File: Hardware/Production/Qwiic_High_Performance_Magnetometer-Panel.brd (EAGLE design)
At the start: 99.3 x 93.9 mm, 420 parts, among them J1 Qwiic, J10 Qwiic, J11 Qwiic, J13 Qwiic, J14 Qwiic, J16 Qwiic, J17 Qwiic, J19 Qwiic, J2 Qwiic, J20 Qwiic, J22 Qwiic, J23 Qwiic, J25 Qwiic, J26 Qwiic, J4 Qwiic, J5 Qwiic, J7 Qwiic, J8 Qwiic, U1 MMC5893MA_QFN16, U2 MMC5893MA_QFN16, U3 MMC5893MA_QFN16, U4 MMC5893MA_QFN16, U5 MMC5893MA_QFN16, U6 MMC5893MA_QFN16, U7 MMC5893MA_QFN16, U8 MMC5893MA_QFN16, U9 MMC5893MA_QFN16

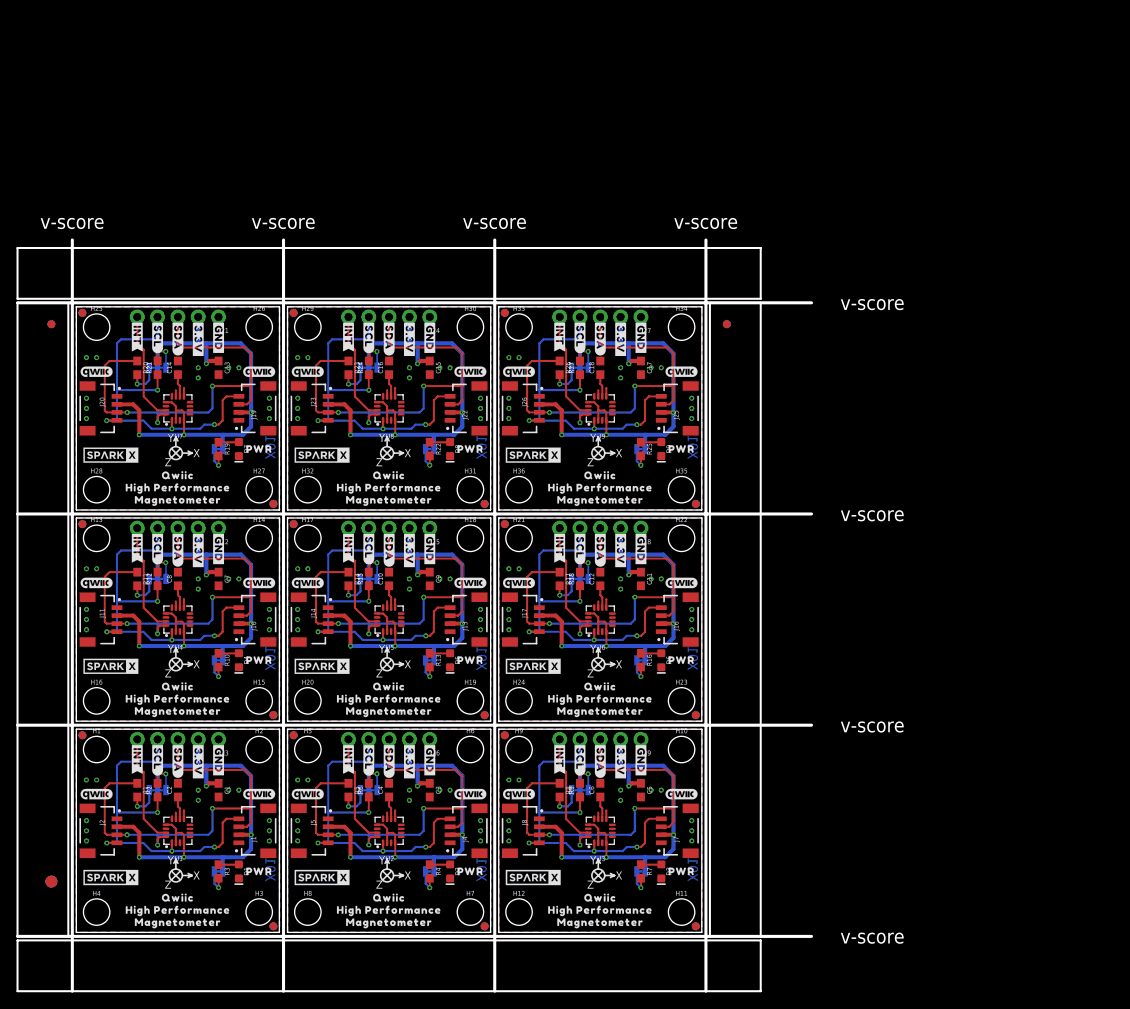
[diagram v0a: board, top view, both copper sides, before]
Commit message: Added SPI breakout header; created PCB production files.
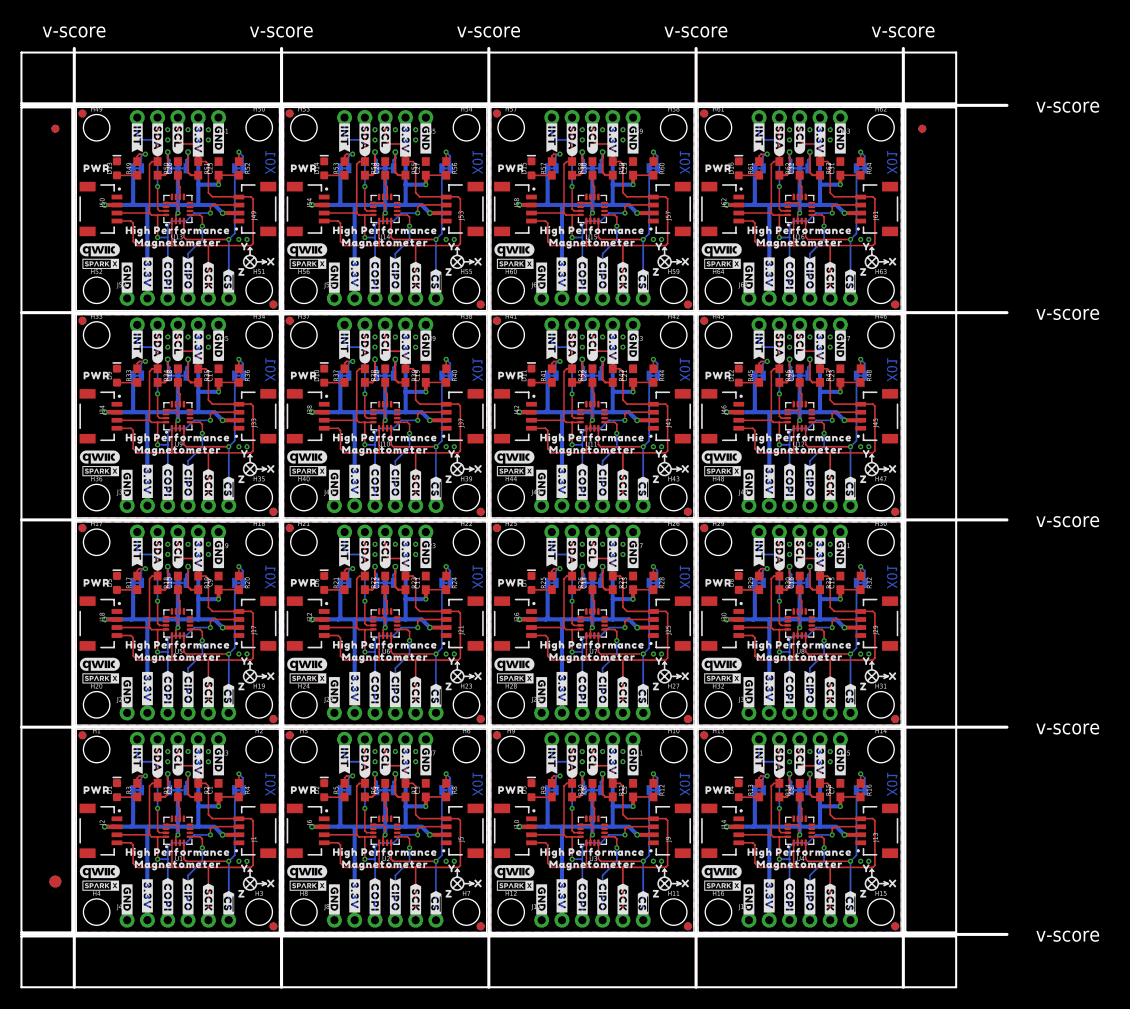
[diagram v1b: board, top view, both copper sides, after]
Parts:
- added C19, C21, C23, C25, C27, C29, C31: 0.1uF, SparkFun-Capacitors:0603
- added C20, C22, C24, C26, C28, C30, C32: 10uF, SparkFun-Capacitors:0603
- added D10, D11, D12, D13, D14, D15, D16: RED, SparkFun-LED:LED-0603
- added FD37, FD38, FD39, FD40, FD41, FD42, FD43, FD44, FD45, FD46, FD47, FD48, FD49, FD50, FD51, FD52, FD53, FD54, FD55, FD56, FD57, FD58, FD59, FD60, FD61, FD62, FD63, FD64: FIDUCIAL1X2, SparkFun-Aesthetics:FIDUCIAL-1X2
- added FRAME10, FRAME11, FRAME12, FRAME13, FRAME14, FRAME15, FRAME16: FRAME-LETTERNO_PACKAGE, SparkFun-Aesthetics:DUMMY
- added H37, H38, H39, H40, H41, H42, H43, H44, H45, H46, H47, H48, H49, H50, H51, H52, H53, H54, H55, H56, H57, H58, H59, H60, H61, H62, H63, H64: STAND-OFF, SparkFun-Hardware:STAND-OFF
- added J28, J32, J36, J40, J44, J48, J52, J56, J60, J64: (no value), SparkFun-Connectors:1X06_NO_SILK
- added J29, J30, J33, J34, J37, J38, J41, J42, J45, J46, J49, J50, J53, J54, J57, J58, J61, J62: Qwiic, SparkFun-Connectors:JST04_1MM_RA
- added J31, J35, J39, J43, J47, J51, J55, J59, J63: (no value), SparkFun-Connectors:1X05_NO_SILK
- added JP19, JP21, JP22, JP24, JP25, JP27, JP28, JP30, JP31, JP33, JP34, JP36, JP37, JP39, JP40, JP42, JP43, JP45, JP46, JP48: JUMPER-SMT_2_NC_TRACE_SILK, SparkFun-Jumpers:SMT-JUMPER_2_NC_TRACE_SILK
- added JP20, JP23, JP26, JP29, JP32, JP35, JP38, JP41, JP44, JP47: JUMPER-SMT_3_2-NC_TRACE_SILK, SparkFun-Jumpers:SMT-JUMPER_3_2-NC_TRACE_SILK
- added LOGO28, LOGO31, LOGO34, LOGO37, LOGO40, LOGO43, LOGO46: OSHW-LOGOMINI, SparkFun-Aesthetics:OSHW-LOGO-MINI
- added LOGO29, LOGO30, LOGO32, LOGO33, LOGO35, LOGO36, LOGO38, LOGO39, LOGO41, LOGO42, LOGO44, LOGO45, LOGO47, LOGO48: QWIIC_LOGO_5MM, SparkFun-Aesthetics:QWIIC_5MM
- added R28, R32, R36, R40, R44, R48, R52, R56, R60, R64: 10k, SparkFun-Resistors:0603
- added R29, R33, R37, R41, R45, R49, R53, R57, R61: 1k, SparkFun-Resistors:0603
- added R30, R31, R34, R35, R38, R39, R42, R43, R46, R47, R50, R51, R54, R55, R58, R59, R62, R63: 2.2k, SparkFun-Resistors:0603
- added U$199, U$238, U$277, U$316, U$355, U$394, U$433, U$472, U$511, U$550, U$589: (no value), output:PWR9
- added U$200, U$221, U$239, U$260, U$278, U$299, U$317, U$338, U$356, U$377, U$395, U$416, U$434, U$455, U$473, U$494, U$512, U$533, U$551, U$572, U$590, U$611: (no value), output:HIGH_PERFORMANCE11
- added U$201, U$222, U$240, U$261, U$279, U$300, U$318, U$339, U$357, U$378, U$396, U$417, U$435, U$456, U$474, U$495, U$513, U$534, U$552, U$573, U$591, U$612: (no value), output:MAGNETOMETER12
- added U$202, U$214, U$224, U$235, U$241, U$253, U$263, U$274, U$280, U$292, U$302, U$313, U$319, U$331, U$341, U$352, U$358, U$370, U$380, U$391, U$397, U$409, U$419, U$430, U$436, U$448, U$458, U$469, U$475, U$487, U$497, U$508, U$514, U$526, U$536, U$547, U$553, U$565, U$575, U$586, U$592, U$604, U$614: (no value), output:#3#3V#0
- added U$203, U$220, U$223, U$236, U$242, U$259, U$262, U$275, U$281, U$298, U$301, U$314, U$320, U$337, U$340, U$353, U$359, U$376, U$379, U$392, U$398, U$415, U$418, U$431, U$437, U$454, U$457, U$470, U$476, U$493, U$496, U$509, U$515, U$532, U$535, U$548, U$554, U$571, U$574, U$587, U$593, U$610, U$613: (no value), output:#GND#4
- added U$204, U$237, U$243, U$276, U$282, U$315, U$321, U$354, U$360, U$393, U$399, U$432, U$438, U$471, U$477, U$510, U$516, U$549, U$555, U$588, U$594: (no value), output:#INT#7
- added U$205, U$244, U$283, U$322, U$361, U$400, U$439, U$478, U$517, U$556, U$595: (no value), output:#LED#8
- added U$206, U$245, U$284, U$323, U$362, U$401, U$440, U$479, U$518, U$557, U$596: (no value), output:#I2C#9
- added U$207, U$246, U$285, U$324, U$363, U$402, U$441, U$480, U$519, U$558, U$597: (no value), output:#SPI#9
- added U$208, U$232, U$247, U$271, U$286, U$310, U$325, U$349, U$364, U$388, U$403, U$427, U$442, U$466, U$481, U$505, U$520, U$544, U$559, U$583, U$598, U$622: (no value), output:#SCL#6
- added U$209, U$233, U$248, U$272, U$287, U$311, U$326, U$350, U$365, U$389, U$404, U$428, U$443, U$467, U$482, U$506, U$521, U$545, U$560, U$584, U$599, U$623: (no value), output:#SDA#5
- added U$210, U$226, U$249, U$265, U$288, U$304, U$327, U$343, U$366, U$382, U$405, U$421, U$444, U$460, U$483, U$499, U$522, U$538, U$561, U$577, U$600, U$616: (no value), output:#CIPO#11
- added U$211, U$225, U$250, U$264, U$289, U$303, U$328, U$342, U$367, U$381, U$406, U$420, U$445, U$459, U$484, U$498, U$523, U$537, U$562, U$576, U$601, U$615: (no value), output:#COPI#12
- added U$212, U$227, U$251, U$266, U$290, U$305, U$329, U$344, U$368, U$383, U$407, U$422, U$446, U$461, U$485, U$500, U$524, U$539, U$563, U$578, U$602, U$617: (no value), output:#SCK#13
- added U$213, U$228, U$252, U$267, U$291, U$306, U$330, U$345, U$369, U$384, U$408, U$423, U$447, U$462, U$486, U$501, U$525, U$540, U$564, U$579, U$603, U$618: (no value), output:##CS##10
- added U$215, U$218, U$254, U$257, U$293, U$296, U$332, U$335, U$371, U$374, U$410, U$413, U$449, U$452, U$488, U$491, U$527, U$530, U$566, U$569, U$605, U$608: (no value), output:Y16
- added U$216, U$217, U$255, U$256, U$294, U$295, U$333, U$334, U$372, U$373, U$411, U$412, U$450, U$451, U$489, U$490, U$528, U$529, U$567, U$568, U$606, U$607: (no value), output:X15
- added U$219, U$234, U$258, U$273, U$297, U$312, U$336, U$351, U$375, U$390, U$414, U$429, U$453, U$468, U$492, U$507, U$531, U$546, U$570, U$585, U$609, U$624: (no value), output:Z17
- added U$229, U$268, U$307, U$346, U$385, U$424, U$463, U$502, U$541, U$580, U$619: SPARKX-LOGO2, SparkX:SPARKX-TINY
- added U$230, U$269, U$308, U$347, U$386, U$425, U$464, U$503, U$542, U$581, U$620: SPARKX-LOGO3, SparkX:SPARKX-SMALL
- added U$231, U$270, U$309, U$348, U$387, U$426, U$465, U$504, U$543, U$582, U$621: (no value), output:MADE_IN_THE_USA20
- added U10, U11, U12, U13, U14, U15, U16: MMC5893MA_QFN16, SparkFun-Sensors:LGA-16-3X3MM-4X4PINS
- J11, J19, J23, J7: value Qwiic -> (none); device SparkFun-Connectors:JST04_1MM_RA -> SparkFun-Connectors:1X05_NO_SILK
- J12, J24: device SparkFun-Connectors:1X05_NO_SILK -> SparkFun-Connectors:1X06_NO_SILK
- J16, J20, J4, J8: value Qwiic -> (none); device SparkFun-Connectors:JST04_1MM_RA -> SparkFun-Connectors:1X06_NO_SILK
- J18, J21, J6, J9: value (none) -> Qwiic; device SparkFun-Connectors:1X05_NO_SILK -> SparkFun-Connectors:JST04_1MM_RA
- JP10, JP12, JP16, JP18, JP4, JP6: value JUMPER-SMT_3_2-NC_TRACE_SILK -> JUMPER-SMT_2_NC_TRACE_SILK; device SparkFun-Jumpers:SMT-JUMPER_3_2-NC_TRACE_SILK -> SparkFun-Jumpers:SMT-JUMPER_2_NC_TRACE_SILK
- JP11, JP17, JP5: value JUMPER-SMT_2_NC_TRACE_SILK -> JUMPER-SMT_3_2-NC_TRACE_SILK; device SparkFun-Jumpers:SMT-JUMPER_2_NC_TRACE_SILK -> SparkFun-Jumpers:SMT-JUMPER_3_2-NC_TRACE_SILK
- LOGO11, LOGO12, LOGO14, LOGO15, LOGO17, LOGO18, LOGO2, LOGO20, LOGO21, LOGO23, LOGO24, LOGO26, LOGO27, LOGO3, LOGO5, LOGO6, LOGO8, LOGO9: value QWIIC_LOGO_4MM -> QWIIC_LOGO_5MM; device SparkFun-Aesthetics:QWIIC_4MM -> SparkFun-Aesthetics:QWIIC_5MM
- R10, R19, R22, R7: value 1k -> 2.2k
- R12, R20, R24, R8: value 2.2k -> 10k
- R16, R4: value 1k -> 10k
- R17, R21, R5, R9: value 2.2k -> 1k
- U$1: value SPARKX-LOGO5 -> (none); device SparkX:SPARKX-LARGE -> output:HIGH_PERFORMANCE11
- U$100, U$25: device output:#3#3V#0 -> output:X15
- U$101, U$26: device output:#GND#4 -> output:Y16
- U$102, U$27: device output:#SCL#6 -> output:Z17
- U$103, U$125, U$28: device output:#SDA#5 -> output:#GND#4
- U$104, U$161: device output:#INT#7 -> output:HIGH_PERFORMANCE11
- U$105: device output:QWIIC10 -> output:MAGNETOMETER12
- U$106, U$142, U$164: device output:HIGH_PERFORMANCE11 -> output:#GND#4
- U$107, U$85: device output:MAGNETOMETER12 -> output:#3#3V#0
- U$108: device output:MADE_IN_THE_USA13 -> output:#COPI#12
- U$109: device output:#LED#8 -> output:#CIPO#11
- U$110: device output:#I2C#9 -> output:#SCK#13
- U$111: value SPARKX-LOGO5 -> (none); device SparkX:SPARKX-LARGE -> output:##CS##10
- U$112: value SPARKX-LOGO3 -> SPARKX-LOGO2; device SparkX:SPARKX-SMALL -> SparkX:SPARKX-TINY
- U$113: value (none) -> SPARKX-LOGO3; device output:#3#3V#0 -> SparkX:SPARKX-SMALL
- U$114: device output:#GND#4 -> output:MADE_IN_THE_USA20
- U$117: device output:#INT#7 -> output:Z17
- U$118: device output:PWR9 -> output:#3#3V#0
- U$119: device output:QWIIC10 -> output:#GND#4
- U$120: device output:HIGH_PERFORMANCE11 -> output:#INT#7
- U$121: device output:MAGNETOMETER12 -> output:PWR9
- U$122: device output:#3#3V#0 -> output:HIGH_PERFORMANCE11
- U$123: device output:#GND#4 -> output:MAGNETOMETER12
- U$124, U$146, U$58: device output:#SCL#6 -> output:#3#3V#0
- U$127: device output:QWIIC10 -> output:#LED#8
- U$128: device output:HIGH_PERFORMANCE11 -> output:#I2C#9
- U$129: device output:MAGNETOMETER12 -> output:#SPI#9
- U$130: device output:MADE_IN_THE_USA13 -> output:#SCL#6
- U$131: device output:#LED#8 -> output:#SDA#5
- U$132: device output:#I2C#9 -> output:#CIPO#11
- U$133: value SPARKX-LOGO5 -> (none); device SparkX:SPARKX-LARGE -> output:#COPI#12
- U$134: value SPARKX-LOGO3 -> (none); device SparkX:SPARKX-SMALL -> output:#SCK#13
- U$135: device output:#3#3V#0 -> output:##CS##10
- U$136, U$79: device output:#GND#4 -> output:#3#3V#0
- U$137: device output:#SCL#6 -> output:Y16
- U$138: device output:#SDA#5 -> output:X15
- U$139, U$60: device output:#INT#7 -> output:X15
- U$14, U$71: device output:#SCL#6 -> output:#SCK#13
- U$140: device output:PWR9 -> output:Y16
- U$141, U$39: device output:QWIIC10 -> output:Z17
- U$143: device output:MAGNETOMETER12 -> output:HIGH_PERFORMANCE11
- U$144: device output:#3#3V#0 -> output:MAGNETOMETER12
- U$147, U$94: device output:#SDA#5 -> output:#COPI#12
- U$148: device output:#INT#7 -> output:#CIPO#11
- U$149: device output:QWIIC10 -> output:#SCK#13
- U$15, U$72: device output:#SDA#5 -> output:##CS##10
- U$150: device output:HIGH_PERFORMANCE11 -> output:##CS##10
- U$151: value (none) -> SPARKX-LOGO2; device output:MAGNETOMETER12 -> SparkX:SPARKX-TINY
- U$152: value (none) -> SPARKX-LOGO3; device output:MADE_IN_THE_USA13 -> SparkX:SPARKX-SMALL
- U$153: device output:#LED#8 -> output:MADE_IN_THE_USA20
- U$154: device output:#I2C#9 -> output:#SCL#6
- U$155: value SPARKX-LOGO5 -> (none); device SparkX:SPARKX-LARGE -> output:#SDA#5
- U$156: value SPARKX-LOGO3 -> (none); device SparkX:SPARKX-SMALL -> output:Z17
- U$159: device output:#SCL#6 -> output:#INT#7
- U$160: device output:#SDA#5 -> output:PWR9
- U$162: device output:PWR9 -> output:MAGNETOMETER12
- U$163, U$18, U$185, U$97: device output:QWIIC10 -> output:#3#3V#0
- U$165: device output:MAGNETOMETER12 -> output:#INT#7
- U$166: device output:#3#3V#0 -> output:#LED#8
- U$167: device output:#GND#4 -> output:#I2C#9
- U$168: device output:#SCL#6 -> output:#SPI#9
- U$169: device output:#SDA#5 -> output:#SCL#6
- U$17, U$64, U$86: device output:MADE_IN_THE_USA13 -> output:#GND#4
- U$170, U$38: device output:#INT#7 -> output:#SDA#5
- U$171, U$31: device output:QWIIC10 -> output:#CIPO#11
- U$172, U$186: device output:HIGH_PERFORMANCE11 -> output:#COPI#12
- U$173: device output:MAGNETOMETER12 -> output:#SCK#13
- U$174: device output:MADE_IN_THE_USA13 -> output:##CS##10
- U$175: device output:#LED#8 -> output:#3#3V#0
- U$176: device output:#I2C#9 -> output:Y16
- U$177: value SPARKX-LOGO5 -> (none); device SparkX:SPARKX-LARGE -> output:X15
- U$178: value SPARKX-LOGO3 -> (none); device SparkX:SPARKX-SMALL -> output:X15
- U$179: device output:#3#3V#0 -> output:Y16
- U$180: device output:#GND#4 -> output:Z17
- U$181, U$80: device output:#SCL#6 -> output:#GND#4
- U$182: device output:#SDA#5 -> output:HIGH_PERFORMANCE11
- U$183: device output:#INT#7 -> output:MAGNETOMETER12
- U$184: device output:PWR9 -> output:#GND#4
- U$187: device output:MAGNETOMETER12 -> output:#CIPO#11
- U$188, U$56: device output:#3#3V#0 -> output:#SCK#13
- U$189, U$57: device output:#GND#4 -> output:##CS##10
- U$19, U$62, U$98: device output:HIGH_PERFORMANCE11 -> output:Y16
- U$190, U$36: value (none) -> SPARKX-LOGO2; device output:#SCL#6 -> SparkX:SPARKX-TINY
- U$191, U$37: value (none) -> SPARKX-LOGO3; device output:#SDA#5 -> SparkX:SPARKX-SMALL
- U$192: device output:#INT#7 -> output:MADE_IN_THE_USA20
- U$193: device output:QWIIC10 -> output:#SCL#6
- U$194: device output:HIGH_PERFORMANCE11 -> output:#SDA#5
- U$195, U$63: device output:MAGNETOMETER12 -> output:Z17
- U$196: device output:MADE_IN_THE_USA13 -> output:#3#3V#0
- U$197: device output:#LED#8 -> output:#GND#4
- U$198: device output:#I2C#9 -> output:#INT#7
- U$2: value SPARKX-LOGO3 -> (none); device SparkX:SPARKX-SMALL -> output:#SCL#6
- U$20, U$99: device output:MAGNETOMETER12 -> output:X15
- U$23: value SPARKX-LOGO5 -> (none); device SparkX:SPARKX-LARGE -> output:#SPI#9
- U$24: value SPARKX-LOGO3 -> (none); device SparkX:SPARKX-SMALL -> output:MAGNETOMETER12
- U$29: device output:#INT#7 -> output:#3#3V#0
- U$30: device output:PWR9 -> output:#COPI#12
- U$32: device output:HIGH_PERFORMANCE11 -> output:#SCK#13
- U$33: device output:MAGNETOMETER12 -> output:##CS##10
- U$34: device output:#3#3V#0 -> output:MADE_IN_THE_USA20
- U$35: device output:#GND#4 -> output:#SCL#6
- U$40: device output:HIGH_PERFORMANCE11 -> output:#3#3V#0
- U$41: device output:MAGNETOMETER12 -> output:#GND#4
- U$42: device output:MADE_IN_THE_USA13 -> output:#INT#7
- U$43: device output:#LED#8 -> output:PWR9
- U$44: device output:#I2C#9 -> output:HIGH_PERFORMANCE11
- U$45: value SPARKX-LOGO5 -> (none); device SparkX:SPARKX-LARGE -> output:MAGNETOMETER12
- U$46, U$68: value SPARKX-LOGO3 -> (none); device SparkX:SPARKX-SMALL -> output:#3#3V#0
- U$47: device output:#3#3V#0 -> output:#GND#4
- U$48: device output:#GND#4 -> output:#INT#7
- U$49: device output:#SCL#6 -> output:#LED#8
- U$5: device output:#SCL#6 -> output:#SDA#5
- U$50: device output:#SDA#5 -> output:#I2C#9
- U$51: device output:#INT#7 -> output:#SPI#9
- U$52: device output:PWR9 -> output:#SCL#6
- U$53: device output:QWIIC10 -> output:#SDA#5
- U$54: device output:HIGH_PERFORMANCE11 -> output:#CIPO#11
- U$55: device output:MAGNETOMETER12 -> output:#COPI#12
- U$59: device output:#SDA#5 -> output:Y16
- U$6: device output:#SDA#5 -> output:#CIPO#11
- U$61: device output:QWIIC10 -> output:X15
- U$65: device output:#LED#8 -> output:HIGH_PERFORMANCE11
- U$66: device output:#I2C#9 -> output:MAGNETOMETER12
- U$67: value SPARKX-LOGO5 -> (none); device SparkX:SPARKX-LARGE -> output:#GND#4
- U$69: device output:#3#3V#0 -> output:#COPI#12
- U$70: device output:#GND#4 -> output:#CIPO#11
- U$73: value (none) -> SPARKX-LOGO2; device output:#INT#7 -> SparkX:SPARKX-TINY
- U$74: value (none) -> SPARKX-LOGO3; device output:PWR9 -> SparkX:SPARKX-SMALL
- U$75: device output:QWIIC10 -> output:MADE_IN_THE_USA20
- U$76: device output:HIGH_PERFORMANCE11 -> output:#SCL#6
- U$77: device output:MAGNETOMETER12 -> output:#SDA#5
- U$78: device output:#3#3V#0 -> output:Z17
- U$81: device output:#SDA#5 -> output:#INT#7
- U$82: device output:#INT#7 -> output:PWR9
- U$83: device output:QWIIC10 -> output:HIGH_PERFORMANCE11
- U$84: device output:HIGH_PERFORMANCE11 -> output:MAGNETOMETER12
- U$87: device output:#LED#8 -> output:#INT#7
- U$88: device output:#I2C#9 -> output:#LED#8
- U$89: value SPARKX-LOGO5 -> (none); device SparkX:SPARKX-LARGE -> output:#I2C#9
- U$9: device output:QWIIC10 -> output:#COPI#12
- U$90: value SPARKX-LOGO3 -> (none); device SparkX:SPARKX-SMALL -> output:#SPI#9
- U$91: device output:#3#3V#0 -> output:#SCL#6
- U$92: device output:#GND#4 -> output:#SDA#5
- U$93: device output:#SCL#6 -> output:#CIPO#11
- U$95: device output:#INT#7 -> output:#SCK#13
- U$96: device output:PWR9 -> output:##CS##10
- moved U$139 115.0 mm to (102.4, 11.4), flipped to the bottom, turned to 0 degrees
- moved U$138 113.8 mm to (102.1, 6.10), turned to 0 degrees
- moved U$148 112.4 mm to (91.7, 1.91)
- moved U$137 112.1 mm to (98.8, 8.00), turned to 0 degrees
- moved U$135 110.5 mm to (96.8, 1.91)
- moved U$134 106.9 mm to (94.2, 1.91), turned to 270 degrees
- moved U$147 106.8 mm to (89.2, 1.91)
- moved U$146 103.5 mm to (86.6, 6.73)
- moved U$150 100.6 mm to (96.8, 1.91), turned to 270 degrees
- moved U$144 100.4 mm to (90.4, 10.0), turned to 0 degrees
- moved U$133 99.6 mm to (89.2, 1.91), flipped to the top, turned to 270 degrees
- moved U$149 99.2 mm to (94.2, 1.91), turned to 270 degrees
- moved U$136 97.9 mm to (86.6, 6.99)
- moved U$141 97.2 mm to (97.8, 10.0), flipped to the bottom
- moved U$145 96.6 mm to (84.1, 6.35)
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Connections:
- removed net N$8 (its old number): JP4.3, R5.2
- removed net SCL: J1.4, J2.4, J3.4, R2.1, U1.1
- removed net SCL1: J4.4, J5.4, J6.4, R6.1, U2.1
- removed net SCL2: J7.4, J8.4, J9.4, R9.1, U3.1
- removed net SCL3: J10.4, J11.4, J12.4, R12.1, U4.1
- removed net SCL4: J13.4, J14.4, J15.4, R15.1, U5.1
- removed net SCL5: J16.4, J17.4, J18.4, R18.1, U6.1
- removed net SCL6: J19.4, J20.4, J21.4, R21.1, U7.1
- removed net SCL7: J22.4, J23.4, J24.4, R24.1, U8.1
- removed net SCL8: J25.4, J26.4, J27.4, R27.1, U9.1
- removed net SDA: J1.3, J2.3, J3.3, R1.1, U1.16
- removed net SDA1: J4.3, J5.3, J6.3, R5.1, U2.16
- removed net SDA2: J7.3, J8.3, J9.3, R8.1, U3.16
- removed net SDA3: J10.3, J11.3, J12.3, R11.1, U4.16
- removed net SDA4: J13.3, J14.3, J15.3, R14.1, U5.16
- removed net SDA5: J16.3, J17.3, J18.3, R17.1, U6.16
- removed net SDA6: J19.3, J20.3, J21.3, R20.1, U7.16
- removed net SDA7: J22.3, J23.3, J24.3, R23.1, U8.16
- removed net SDA8: J25.3, J26.3, J27.3, R26.1, U9.16
- new net !CS!: J4.6, JP2.1, U1.4
- new net !CS!1: J8.6, JP6.1, U2.4
- new net !CS!10: J44.6, JP33.1, U11.4
- new net !CS!11: J48.6, JP36.1, U12.4
- new net !CS!12: J52.6, JP39.1, U13.4
- new net !CS!13: J56.6, JP42.1, U14.4
- new net !CS!14: J60.6, JP45.1, U15.4
- new net !CS!15: J64.6, JP48.1, U16.4
- new net !CS!2: J12.6, JP9.1, U3.4
- new net !CS!3: J16.6, JP12.1, U4.4
- new net !CS!4: J20.6, JP15.1, U5.4
- new net !CS!5: J24.6, JP18.1, U6.4
- new net !CS!6: J28.6, JP21.1, U7.4
- new net !CS!7: J32.6, JP24.1, U8.4
- new net !CS!8: J36.6, JP27.1, U9.4
- new net !CS!9: J40.6, JP30.1, U10.4
- new net 3.3V10: C21.1, J41.2, J42.2, J43.2, J44.2, JP31.2, JP32.2, R44.2, U11.13, U11.2
- new net 3.3V11: C23.1, J45.2, J46.2, J47.2, J48.2, JP34.2, JP35.2, R48.2, U12.13, U12.2
- new net 3.3V12: C25.1, J49.2, J50.2, J51.2, J52.2, JP37.2, JP38.2, R52.2, U13.13, U13.2
- new net 3.3V13: C27.1, J53.2, J54.2, J55.2, J56.2, JP40.2, JP41.2, R56.2, U14.13, U14.2
- new net 3.3V14: C29.1, J57.2, J58.2, J59.2, J60.2, JP43.2, JP44.2, R60.2, U15.13, U15.2
- new net 3.3V15: C31.1, J61.2, J62.2, J63.2, J64.2, JP46.2, JP47.2, R64.2, U16.13, U16.2
- new net 3.3V9: C19.1, J37.2, J38.2, J39.2, J40.2, JP28.2, JP29.2, R40.2, U10.13, U10.2
- new net CAP10: C22.1, U11.10
- new net CAP11: C24.1, U12.10
- new net CAP12: C26.1, U13.10
- new net CAP13: C28.1, U14.10
- new net CAP14: C30.1, U15.10
- new net CAP15: C32.1, U16.10
- new net CAP9: C20.1, U10.10
- new net CIPO: J4.4, U1.5
- new net CIPO1: J8.4, U2.5
- new net CIPO10: J44.4, U11.5
- new net CIPO11: J48.4, U12.5
- new net CIPO12: J52.4, U13.5
- new net CIPO13: J56.4, U14.5
- new net CIPO14: J60.4, U15.5
- new net CIPO15: J64.4, U16.5
- new net CIPO2: J12.4, U3.5
- new net CIPO3: J16.4, U4.5
- new net CIPO4: J20.4, U5.5
- new net CIPO5: J24.4, U6.5
- new net CIPO6: J28.4, U7.5
- new net CIPO7: J32.4, U8.5
- new net CIPO8: J36.4, U9.5
- new net CIPO9: J40.4, U10.5
- new net GND10: C21.2, C22.2, D11.C, J41.1, J42.1, J43.1, J44.1, U11.11, U11.9
- new net GND11: C23.2, C24.2, D12.C, J45.1, J46.1, J47.1, J48.1, U12.11, U12.9
- new net GND12: C25.2, C26.2, D13.C, J49.1, J50.1, J51.1, J52.1, U13.11, U13.9
- new net GND13: C27.2, C28.2, D14.C, J53.1, J54.1, J55.1, J56.1, U14.11, U14.9
- new net GND14: C29.2, C30.2, D15.C, J57.1, J58.1, J59.1, J60.1, U15.11, U15.9
- new net GND15: C31.2, C32.2, D16.C, J61.1, J62.1, J63.1, J64.1, U16.11, U16.9
- new net GND9: C19.2, C20.2, D10.C, J37.1, J38.1, J39.1, J40.1, U10.11, U10.9
- new net INT10: J43.5, U11.15
- new net INT11: J47.5, U12.15
- new net INT12: J51.5, U13.15
- new net INT13: J55.5, U14.15
- new net INT14: J59.5, U15.15
- new net INT15: J63.5, U16.15
- new net INT9: J39.5, U10.15
- new net N$37: D8.A, R29.1
- new net N$38: JP23.1, R31.2
- new net N$39: JP23.3, R30.2
- new net N$40: JP24.2, R32.1
- new net N$41: JP25.1, R33.2
- new net N$42: D9.A, R33.1
- new net N$43: JP26.1, R35.2
- new net N$44: JP26.3, R34.2
- new net N$45: JP27.2, R36.1
- new net N$46: JP28.1, R37.2
- new net N$47: D10.A, R37.1
- new net N$48: JP29.1, R39.2
- new net N$49: JP29.3, R38.2
- new net N$50: JP30.2, R40.1
- new net N$51: JP31.1, R41.2
- new net N$52: D11.A, R41.1
- new net N$53: JP32.1, R43.2
- new net N$54: JP32.3, R42.2
- new net N$55: JP33.2, R44.1
- new net N$56: JP34.1, R45.2
- new net N$57: D12.A, R45.1
- new net N$58: JP35.1, R47.2
- new net N$59: JP35.3, R46.2
- new net N$60: JP36.2, R48.1
- new net N$61: JP37.1, R49.2
- new net N$62: D13.A, R49.1
- new net N$63: JP38.1, R51.2
- new net N$64: JP38.3, R50.2
- new net N$65: JP39.2, R52.1
- new net N$66: JP40.1, R53.2
- new net N$67: D14.A, R53.1
- new net N$68: JP41.1, R55.2
- new net N$69: JP41.3, R54.2
- new net N$70: JP42.2, R56.1
- new net N$71: JP43.1, R57.2
- new net N$72: D15.A, R57.1
- new net N$73: JP44.1, R59.2
- new net N$74: JP44.3, R58.2
- new net N$75: JP45.2, R60.1
- new net N$76: JP46.1, R61.2
- new net N$77: D16.A, R61.1
- new net N$78: JP47.1, R63.2
- new net N$79: JP47.3, R62.2
- new net N$80: JP48.2, R64.1
- new net N$9: JP5.3, R6.2
- new net SCL/SCK: J1.4, J2.4, J3.3, J4.5, R2.1, U1.1
- new net SCL/SCK1: J5.4, J6.4, J7.3, J8.5, R7.1, U2.1
- new net SCL/SCK10: J41.4, J42.4, J43.3, J44.5, R43.1, U11.1
- new net SCL/SCK11: J45.4, J46.4, J47.3, J48.5, R47.1, U12.1
- new net SCL/SCK12: J49.4, J50.4, J51.3, J52.5, R51.1, U13.1
- new net SCL/SCK13: J53.4, J54.4, J55.3, J56.5, R55.1, U14.1
- new net SCL/SCK14: J57.4, J58.4, J59.3, J60.5, R59.1, U15.1
- new net SCL/SCK15: J61.4, J62.4, J63.3, J64.5, R63.1, U16.1
- new net SCL/SCK2: J10.4, J11.3, J12.5, J9.4, R11.1, U3.1
- new net SCL/SCK3: J13.4, J14.4, J15.3, J16.5, R15.1, U4.1
- new net SCL/SCK4: J17.4, J18.4, J19.3, J20.5, R19.1, U5.1
- new net SCL/SCK5: J21.4, J22.4, J23.3, J24.5, R23.1, U6.1
- new net SCL/SCK6: J25.4, J26.4, J27.3, J28.5, R27.1, U7.1
- new net SCL/SCK7: J29.4, J30.4, J31.3, J32.5, R31.1, U8.1
- new net SCL/SCK8: J33.4, J34.4, J35.3, J36.5, R35.1, U9.1
- new net SCL/SCK9: J37.4, J38.4, J39.3, J40.5, R39.1, U10.1
- new net SDA/COPI: J1.3, J2.3, J3.4, J4.3, R1.1, U1.16
- new net SDA/COPI1: J5.3, J6.3, J7.4, J8.3, R6.1, U2.16
- new net SDA/COPI10: J41.3, J42.3, J43.4, J44.3, R42.1, U11.16
- new net SDA/COPI11: J45.3, J46.3, J47.4, J48.3, R46.1, U12.16
- new net SDA/COPI12: J49.3, J50.3, J51.4, J52.3, R50.1, U13.16
- new net SDA/COPI13: J53.3, J54.3, J55.4, J56.3, R54.1, U14.16
- new net SDA/COPI14: J57.3, J58.3, J59.4, J60.3, R58.1, U15.16
- new net SDA/COPI15: J61.3, J62.3, J63.4, J64.3, R62.1, U16.16
- new net SDA/COPI2: J10.3, J11.4, J12.3, J9.3, R10.1, U3.16
- new net SDA/COPI3: J13.3, J14.3, J15.4, J16.3, R14.1, U4.16
- new net SDA/COPI4: J17.3, J18.3, J19.4, J20.3, R18.1, U5.16
- new net SDA/COPI5: J21.3, J22.3, J23.4, J24.3, R22.1, U6.16
- new net SDA/COPI6: J25.3, J26.3, J27.4, J28.3, R26.1, U7.16
- new net SDA/COPI7: J29.3, J30.3, J31.4, J32.3, R30.1, U8.16
- new net SDA/COPI8: J33.3, J34.3, J35.4, J36.3, R34.1, U9.16
- new net SDA/COPI9: J37.3, J38.3, J39.4, J40.3, R38.1, U10.16
- net 3.3V: now also J4.2, R4.2; no longer U1.4
- net 3.3V1: now also J7.2, J8.2, JP5.2, R8.2; no longer J4.2, JP2.2, U2.4
- net 3.3V2: now also J10.2, J11.2, J12.2, JP7.2, JP8.2, R12.2; no longer J7.2, J8.2, JP5.2, JP6.2, U3.4
- net 3.3V3: now also J13.2, J14.2, J15.2, J16.2, JP10.2, JP11.2, R16.2; no longer J10.2, J11.2, J12.2, JP7.2, JP8.2, U4.4
- net 3.3V4: now also J17.2, J18.2, J19.2, J20.2, JP13.2, JP14.2, R20.2; no longer J13.2, J14.2, J15.2, JP10.2, JP9.2, U5.4
- net 3.3V5: now also J21.2, J22.2, J23.2, J24.2, JP16.2, JP17.2, R24.2; no longer J16.2, J17.2, J18.2, JP11.2, JP12.2, U6.4
- net 3.3V6: now also J25.2, J26.2, J27.2, J28.2, JP19.2, JP20.2, R28.2; no longer J19.2, J20.2, J21.2, JP13.2, JP14.2, U7.4
- net 3.3V7: now also J29.2, J30.2, J31.2, J32.2, JP22.2, JP23.2, R32.2; no longer J22.2, J23.2, J24.2, JP15.2, JP16.2, U8.4
- net 3.3V8: now also J33.2, J34.2, J35.2, J36.2, JP25.2, JP26.2, R36.2; no longer J25.2, J26.2, J27.2, JP17.2, JP18.2, U9.4
- net GND: now also J4.1
- net GND1: now also J7.1, J8.1; no longer J4.1
- net GND2: now also J10.1, J11.1, J12.1; no longer J7.1, J8.1
- net GND3: now also J13.1, J14.1, J15.1, J16.1; no longer J10.1, J11.1, J12.1
- net GND4: now also J17.1, J18.1, J19.1, J20.1; no longer J13.1, J14.1, J15.1
- net GND5: now also J21.1, J22.1, J23.1, J24.1; no longer J16.1, J17.1, J18.1
- net GND6: now also J25.1, J26.1, J27.1, J28.1; no longer J19.1, J20.1, J21.1
- net GND7: now also J29.1, J30.1, J31.1, J32.1; no longer J22.1, J23.1, J24.1
- net GND8: now also J33.1, J34.1, J35.1, J36.1; no longer J25.1, J26.1, J27.1
- net INT1: now also J7.5; no longer J6.5
- net INT2: now also J11.5; no longer J9.5
- net INT3: now also J15.5; no longer J12.5
- net INT4: now also J19.5; no longer J15.5
- net INT5: now also J23.5; no longer J18.5
- net INT6: now also J27.5; no longer J21.5
- net INT7: now also J31.5; no longer J24.5
- net INT8: now also J35.5; no longer J27.5
- net N$10: now also JP6.2, R8.1; no longer D3.A, R7.1
- net N$11: now also JP7.1; no longer JP6.1
- net N$12: now also D3.A, R9.1; no longer JP6.3, R8.2
- net N$13: now also JP8.1, R11.2; no longer JP7.1, R10.2
- net N$14: now also JP8.3, R10.2; no longer D4.A, R10.1
- net N$15: now also JP9.2, R12.1; no longer JP8.1, R12.2
- net N$16: now also JP10.1, R13.2; no longer JP8.3, R11.2
- net N$17: now also D4.A, R13.1; no longer JP9.1, R13.2
- net N$18: now also JP11.1, R15.2; no longer D5.A, R13.1
- net N$19: now also JP11.3, R14.2; no longer JP10.1, R15.2
- net N$20: now also JP12.2, R16.1; no longer JP10.3, R14.2
- net N$21: now also JP13.1, R17.2; no longer JP11.1, R16.2
- net N$22: now also D5.A, R17.1; no longer D6.A, R16.1
- net N$23: now also JP14.1, R19.2; no longer JP12.1, R18.2
- net N$24: now also JP14.3, R18.2; no longer JP12.3, R17.2
- net N$25: now also JP15.2, R20.1; no longer JP13.1, R19.2
- net N$26: now also JP16.1, R21.2; no longer D7.A, R19.1
- net N$27: now also D6.A, R21.1; no longer JP14.1, R21.2
- net N$28: now also JP17.1, R23.2; no longer JP14.3, R20.2
- net N$29: now also JP17.3; no longer JP15.1
- net N$30: now also JP18.2, R24.1; no longer D8.A, R22.1
- net N$31: now also JP19.1, R25.2; no longer JP16.1, R24.2
- net N$32: now also D7.A, R25.1; no longer JP16.3, R23.2
- net N$33: now also JP20.1, R27.2; no longer JP17.1, R25.2
- net N$34: now also JP20.3, R26.2; no longer D9.A, R25.1
- net N$35: now also JP21.2, R28.1; no longer JP18.1, R27.2
- net N$36: now also JP22.1, R29.2; no longer JP18.3, R26.2
- net N$5: now also JP2.2, R4.1; no longer JP2.1, R4.2
- net N$6: now also JP4.1, R5.2; no longer D2.A, R4.1
- net N$7: now also D2.A, R5.1; no longer JP4.1, R6.2
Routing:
- net 3.3V15: track 0.00 -> 61.6 mm, vias 0 -> 4
- net 3.3V11: track 0.00 -> 61.6 mm, vias 0 -> 4
- net 3.3V12: track 0.00 -> 61.6 mm, vias 0 -> 4
- net 3.3V9: track 0.00 -> 61.6 mm, vias 0 -> 4
- net 3.3V14: track 0.00 -> 61.6 mm, vias 0 -> 4
- net 3.3V13: track 0.00 -> 61.6 mm, vias 0 -> 4
- net 3.3V10: track 0.00 -> 61.6 mm, vias 0 -> 4
- net SDA5: track 55.0 -> 0.00 mm, vias 3 -> 0
- net SDA8: track 55.0 -> 0.00 mm, vias 3 -> 0
- net SDA2: track 55.0 -> 0.00 mm, vias 3 -> 0
- net SDA3: track 55.0 -> 0.00 mm, vias 3 -> 0
- net SDA6: track 55.0 -> 0.00 mm, vias 3 -> 0
- net SDA7: track 55.0 -> 0.00 mm, vias 3 -> 0
- net SDA4: track 55.0 -> 0.00 mm, vias 3 -> 0
- net SDA1: track 55.0 -> 0.00 mm, vias 3 -> 0
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- added copper zone on layer 1, net GND10
- added copper zone on layer 16, net GND10
- added copper zone on layer 1, net GND11
- added copper zone on layer 16, net GND11
- added copper zone on layer 1, net GND12
- added copper zone on layer 16, net GND12
- added copper zone on layer 1, net GND13
- added copper zone on layer 16, net GND13
- added copper zone on layer 1, net GND14
- added copper zone on layer 16, net GND14
- added copper zone on layer 1, net GND15
- added copper zone on layer 16, net GND15
- added copper zone on layer 1, net GND9
- added copper zone on layer 16, net GND9
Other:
- board size 99.3 x 93.9 mm -> 123.2 x 117.3 mm
- board text removed: "X"
- board text removed: "Y"
- board text removed: "Z"

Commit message: Fixed SPI header alignment.
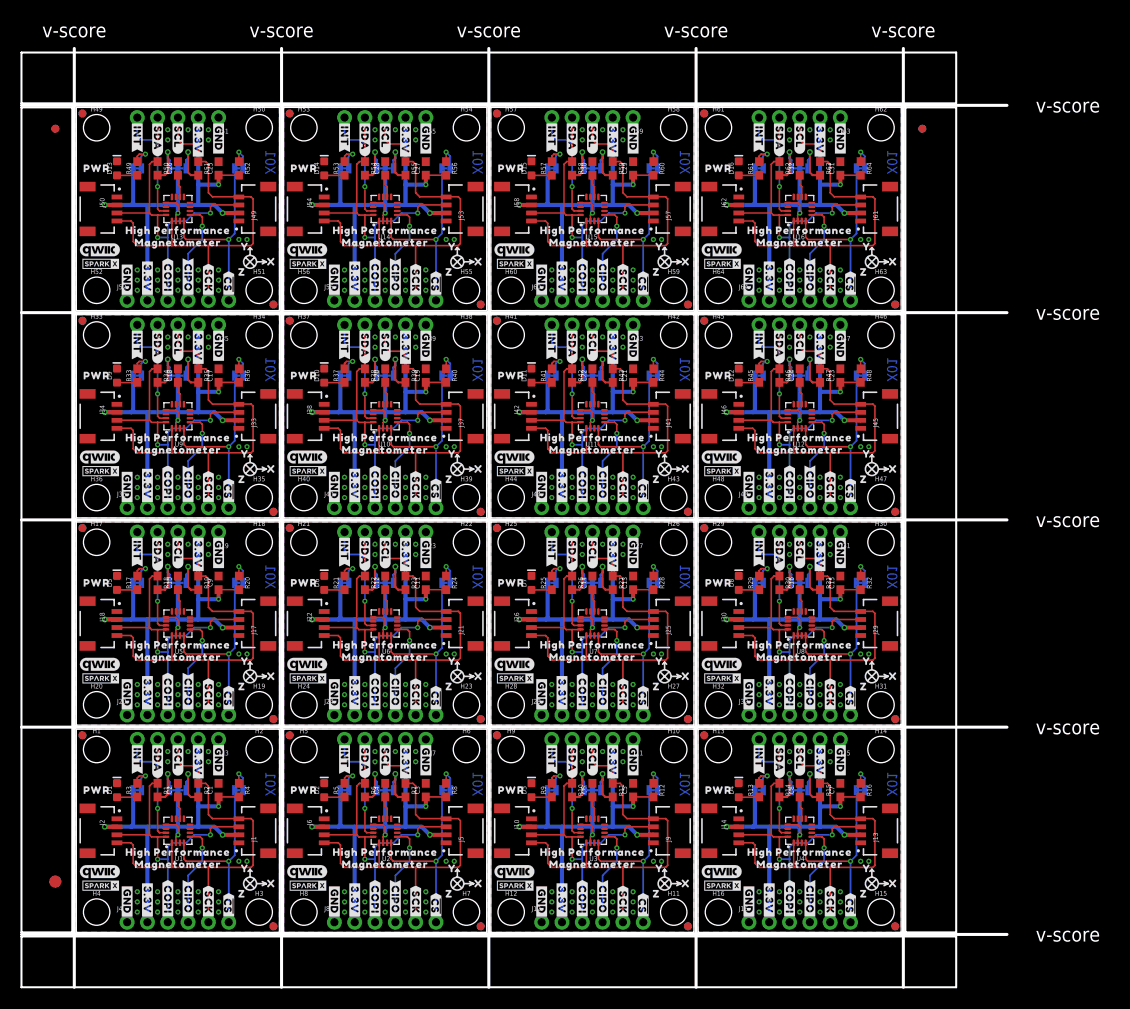
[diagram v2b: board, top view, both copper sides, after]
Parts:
- moved U$487 0.51 mm to (8.89, 84.2)
- moved U$526 0.51 mm to (34.8, 84.2)
- moved U$565 0.51 mm to (60.7, 84.2)
- moved U$604 0.51 mm to (86.6, 84.2)
- moved U$175 0.51 mm to (8.89, 32.4)
- moved U$214 0.51 mm to (34.8, 32.4)
- moved U$253 0.51 mm to (60.7, 32.4)
- moved U$292 0.51 mm to (86.6, 32.4)
- moved U$331 0.51 mm to (8.89, 58.3)
- moved U$370 0.51 mm to (34.8, 58.3)
- moved U$409 0.51 mm to (60.7, 58.3)
- moved U$448 0.51 mm to (86.6, 58.3)
- moved U$136 0.51 mm to (86.6, 6.48)
- moved U$18 0.51 mm to (8.89, 6.48)
- moved U$58 0.51 mm to (34.8, 6.48)
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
